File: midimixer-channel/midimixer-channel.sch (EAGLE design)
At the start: 97 parts, among them IC1 74LS595D, IC2 74LS595D, IC3 74LS595D, IC4 74165D, U1 LM1117IMPX-3.3/NOPB, Y1 8MHz 695-HCM49-8-U

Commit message: wip
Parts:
- removed JP3: (no value), microbuilder:HEADER-1X2ROUND
- removed X1: (no value), keves:TE-292304-1
- added USB: (no value), microbuilder:HEADER-1X4ROUND
- renumbered B1 to USR, B2 to RST
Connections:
- net 5.0V: no longer JP3.1
- net GND: now also USB.4; no longer JP3.2, X1SHIELD.S1, X1SHIELD.S2, X1_CONN.4
- net N$7: now also USB.2; no longer X1_CONN.2
- net N$8: now also USB.3; no longer X1_CONN.3
- net USB_VBUS: now also USB.1; no longer X1_CONN.1
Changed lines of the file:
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@@
 <part name="R12" library="microbuilder" deviceset="RESISTOR" device="_0603" value="10k"/>
 <part name="U$17" library="microbuilder" deviceset="GND" device=""/>
-<part name="X1" library="keves" deviceset="TE-292304-1" device=""/>
-<part name="U$18" library="microbuilder" deviceset="GND" device=""/>
 <part name="U$19" library="microbuilder" deviceset="GND" device=""/>
 <part name="R15" library="microbuilder" deviceset="RESISTOR" device="0603" value="22"/>
@@
 <part name="U$21" library="microbuilder" deviceset="3.3V" device=""/>
 <part name="U$22" library="microbuilder" deviceset="GND" device=""/>
-<part name="JP3" library="microbuilder" deviceset="HEADER-1X2" device="ROUND"/>
 <part name="JP4" library="microbuilder" deviceset="HEADER-1X2" device="ROUND"/>
-<part name="U$23" library="microbuilder" deviceset="GND" device=""/>
 <part name="U$24" library="microbuilder" deviceset="GND" device=""/>
-<part name="U$25" library="microbuilder" deviceset="5.0V" device=""/>
 <part name="U$26" library="microbuilder" deviceset="3.3V" device=""/>
 <part name="U1" library="microbuilder" deviceset="LM1117" device="SOT223-REFLOW" value="LM1117IMPX-3.3/NOPB"/>
@@
 <part name="C19" library="microbuilder" deviceset="CAP_CERAMIC" device="0603" value="0.1uF"/>
 <part name="U$31" library="microbuilder" deviceset="AVDD" device=""/>
-<part name="B2" library="microbuilder" deviceset="SWITCH_TACT_SMT" device=""/>
-<part name="B1" library="microbuilder" deviceset="SWITCH_TACT_SMT" device=""/>
+<part name="RST" library="microbuilder" deviceset="SWITCH_TACT_SMT" device=""/>
+<part name="USR" library="microbuilder" deviceset="SWITCH_TACT_SMT" device=""/>
 <part name="U$32" library="microbuilder" deviceset="GND" device=""/>
 <part name="U$33" library="microbuilder" deviceset="GND" device=""/>
@@
 <part name="U$36" library="microbuilder" deviceset="GND" device=""/>
 <part name="JP5" library="microbuilder" deviceset="HEADER-1X4" device="ROUND"/>
+<part name="USB" library="microbuilder" deviceset="HEADER-1X4" device="ROUND"/>
 </parts>
 <sheets>
@@
 <instance part="R12" gate="G$1" x="88.9" y="101.6"/>
 <instance part="U$17" gate="G$1" x="99.06" y="101.6" rot="R90"/>
-<instance part="X1" gate="_CONN" x="142.24" y="109.22"/>
-<instance part="X1" gate="SHIELD" x="142.24" y="111.76"/>
-<instance part="U$18" gate="G$1" x="144.78" y="96.52"/>
 <instance part="U$19" gate="G$1" x="137.16" y="96.52"/>
 <instance part="R15" gate="G$1" x="129.54" y="111.76"/>
@@
 <instance part="U$21" gate="G$1" x="167.64" y="116.84" rot="R90"/>
 <instance part="U$22" gate="G$1" x="167.64" y="106.68" rot="R270"/>
-<instance part="JP3" gate="G$1" x="180.34" y="93.98"/>
 <instance part="JP4" gate="G$1" x="180.34" y="81.28"/>
-<instance part="U$23" gate="G$1" x="165.1" y="93.98" rot="R270"/>
 <instance part="U$24" gate="G$1" x="165.1" y="81.28" rot="R270"/>
-<instance part="U$25" gate="G$1" x="170.18" y="96.52" rot="R90"/>
 <instance part="U$26" gate="G$1" x="170.18" y="83.82" rot="R90"/>
 <instance part="U1" gate="G$1" x="149.86" y="60.96"/>
@@
 <instance part="C19" gate="G$1" x="205.74" y="53.34"/>
 <instance part="U$31" gate="G$1" x="213.36" y="60.96" rot="R270"/>
-<instance part="B2" gate="G$1" x="147.32" y="27.94" rot="R90"/>
-<instance part="B1" gate="G$1" x="127" y="27.94" rot="R90"/>
+<instance part="RST" gate="G$1" x="147.32" y="27.94" rot="R90"/>
+<instance part="USR" gate="G$1" x="127" y="27.94" rot="R90"/>
 <instance part="U$32" gate="G$1" x="149.86" y="20.32"/>
 <instance part="U$33" gate="G$1" x="129.54" y="20.32"/>
@@
 <instance part="U$36" gate="G$1" x="5.08" y="0" rot="R90"/>
 <instance part="JP5" gate="A" x="-2.54" y="-2.54" rot="R180"/>
+<instance part="USB" gate="A" x="142.24" y="109.22"/>
 </instances>
 <busses>
@@
 </segment>
 <segment>
-<pinref part="X1" gate="SHIELD" pin="S1"/>
-<pinref part="U$18" gate="G$1" pin="GND"/>
-<pinref part="X1" gate="SHIELD" pin="S2"/>
-<wire x1="142.24" y1="99.06" x2="144.78" y2="99.06" width="0.2032" layer="91"/>
-<junction x="144.78" y="99.06"/>
-</segment>
-<segment>
-<pinref part="X1" gate="_CONN" pin="4"/>
 <pinref part="U$19" gate="G$1" pin="GND"/>
 <wire x1="139.7" y1="106.68" x2="137.16" y2="106.68" width="0.2032" layer="91"/>
 <wire x1="137.16" y1="106.68" x2="137.16" y2="99.06" width="0.2032" layer="91"/>
-</segment>
-<segment>
-<pinref part="JP3" gate="G$1" pin="2"/>
-<pinref part="U$23" gate="G$1" pin="GND"/>
-<wire x1="167.64" y1="93.98" x2="177.8" y2="93.98" width="0.1524" layer="91"/>
+<pinref part="USB" gate="A" pin="4"/>
 </segment>
 <segment>
@@
 </segment>
 <segment>
-<pinref part="B2" gate="G$1" pin="P1"/>
+<pinref part="RST" gate="G$1" pin="P1"/>
 <pinref part="U$32" gate="G$1" pin="GND"/>
-<pinref part="B2" gate="G$1" pin="P"/>
+<pinref part="RST" gate="G$1" pin="P"/>
 <wire x1="147.32" y1="22.86" x2="149.86" y2="22.86" width="0.2032" layer="91"/>
 <pinref part="C16" gate="G$1" pin="P$2"/>
@@
 </segment>
 <segment>
-<pinref part="B1" gate="G$1" pin="P1"/>
+<pinref part="USR" gate="G$1" pin="P1"/>
 <pinref part="U$33" gate="G$1" pin="GND"/>
-<pinref part="B1" gate="G$1" pin="P"/>
+<pinref part="USR" gate="G$1" pin="P"/>
 <wire x1="127" y1="22.86" x2="129.54" y2="22.86" width="0.2032" layer="91"/>
 <junction x="129.54" y="22.86"/>
@@
 <wire x1="154.94" y1="30.48" x2="154.94" y2="33.02" width="0.2032" layer="91"/>
 <wire x1="154.94" y1="33.02" x2="149.86" y2="33.02" width="0.2032" layer="91"/>
-<pinref part="B2" gate="G$1" pin="S1"/>
+<pinref part="RST" gate="G$1" pin="S1"/>
 <junction x="149.86" y="33.02"/>
 <wire x1="149.86" y1="33.02" x2="147.32" y2="33.02" width="0.2032" layer="91"/>
-<pinref part="B2" gate="G$1" pin="S"/>
+<pinref part="RST" gate="G$1" pin="S"/>
 <junction x="147.32" y="33.02"/>
 <wire x1="147.32" y1="33.02" x2="139.7" y2="33.02" width="0.2032" layer="91"/>
@@
 <net name="N$7" class="0">
 <segment>
-<pinref part="X1" gate="_CONN" pin="2"/>
 <pinref part="R15" gate="G$1" pin="2"/>
 <wire x1="139.7" y1="111.76" x2="134.62" y2="111.76" width="0.2032" layer="91"/>
+<pinref part="USB" gate="A" pin="2"/>
 </segment>
 </net>
 <net name="N$8" class="0">
 <segment>
-<pinref part="X1" gate="_CONN" pin="3"/>
 <pinref part="R16" gate="G$1" pin="2"/>
 <wire x1="139.7" y1="109.22" x2="134.62" y2="109.22" width="0.2032" layer="91"/>
+<pinref part="USB" gate="A" pin="3"/>
 </segment>
 </net>
@@
 <net name="USB_VBUS" class="0">
 <segment>
-<pinref part="X1" gate="_CONN" pin="1"/>
 <wire x1="139.7" y1="114.3" x2="132.08" y2="114.3" width="0.2032" layer="91"/>
 <label x="114.3" y="114.3" size="1.778" layer="95"/>
@@
 <wire x1="132.08" y1="121.92" x2="132.08" y2="114.3" width="0.2032" layer="91"/>
 <junction x="132.08" y="114.3"/>
+<pinref part="USB" gate="A" pin="1"/>
 </segment>
 <segment>
@@
 <pinref part="JP1" gate="A" pin="1"/>
 <wire x1="124.46" y1="121.92" x2="129.54" y2="121.92" width="0.2032" layer="91"/>
-</segment>
-<segment>
-<pinref part="JP3" gate="G$1" pin="1"/>
-<pinref part="U$25" gate="G$1" pin="5.0V"/>
-<wire x1="172.72" y1="96.52" x2="177.8" y2="96.52" width="0.1524" layer="91"/>
 </segment>
 <segment>
@@
 </segment>
 <segment>
-<pinref part="B1" gate="G$1" pin="S1"/>
+<pinref part="USR" gate="G$1" pin="S1"/>
 <wire x1="129.54" y1="33.02" x2="127" y2="33.02" width="0.2032" layer="91"/>
 <label x="116.84" y="33.02" size="1.778" layer="95"/>
-<pinref part="B1" gate="G$1" pin="S"/>
+<pinref part="USR" gate="G$1" pin="S"/>
 <junction x="127" y="33.02"/>
 <wire x1="127" y1="33.02" x2="119.38" y2="33.02" width="0.2032" layer="91"/>

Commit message: wip
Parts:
- added C26: 0.1uF, microbuilder:CAP_CERAMIC0603
- added IC5: 74165D, SparkFun-DigitalIC:74165D
- added R30, R31, R32, R33, R34, R35, R36, R37, R38: 10k, microbuilder:RESISTOR_0603
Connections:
- removed net DIN_TODO: BTN1.SW2_A, BTN1.SW2_B, C20.P$2
- removed net DIN_TODO2: BTN4.SW2_B, C23.P$2
- removed net N$36: BTN5.SW2_A, BTN5.SW2_B, C24.P$2
- removed net N$41: BTN3.SW2_A, BTN3.SW2_B, C22.P$2
- removed net N$46: BTN6.SW2_B, C25.P$2
- new net DIN_10: BTN1.SW2_A, BTN1.SW2_B, C20.P$2, IC5.B, R36.1
- new net DIN_11: BTN5.SW2_A, BTN5.SW2_B, C24.P$2, IC5.C, R35.1
- new net DIN_12: BTN4.SW2_B, C23.P$2, IC5.D, R34.1
- new net DIN_13: BTN3.SW2_A, BTN3.SW2_B, C22.P$2, IC5.E, R33.1
- new net DIN_14: BTN6.SW2_B, C25.P$2, IC5.F, R32.1
- new net DIN_15: IC5.G, R31.1
- new net DIN_16: IC5.H, R30.1
- new net DIN_9: BTN2.SW2_B, C21.P$2, IC5.A, R37.1
- net 3.3V: now also C26.P$2, IC5.VCC, R30.2, R31.2, R32.2, R33.2, R34.2, R35.2, R36.2, R37.2, R38.2
- net GND: now also C26.P$1, IC5.CLK_INH, IC5.GND
- net N$26: now also IC5.SER, R38.1; no longer BTN2.SW2_B, C21.P$2
- net N$28: now also IC5.QH
- net SPI2_CLK: now also IC5.CLK
- net SPI2_RC2: now also IC5.SH/!LD

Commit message: wip
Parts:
- added JP3: (no value), microbuilder:HEADER-1X3ROUND
- renumbered JP4 to PWR3.3V
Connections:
- removed net N$65: IC1.QH*
- new net UART_RX: CPU1.PC11/SDIO_D3, JP3.2
- new net UART_TX: CPU1.PC10/SDIO_D2, JP3.3
- net GND: now also JP3.1
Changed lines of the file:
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@@
 <part name="U$21" library="microbuilder" deviceset="3.3V" device=""/>
 <part name="U$22" library="microbuilder" deviceset="GND" device=""/>
-<part name="JP4" library="microbuilder" deviceset="HEADER-1X2" device="ROUND"/>
+<part name="PWR3.3V" library="microbuilder" deviceset="HEADER-1X2" device="ROUND"/>
 <part name="U$24" library="microbuilder" deviceset="GND" device=""/>
 <part name="U$26" library="microbuilder" deviceset="3.3V" device=""/>
@@
 <part name="R38" library="microbuilder" deviceset="RESISTOR" device="_0603" value="10k"/>
 <part name="U$47" library="microbuilder" deviceset="3.3V" device=""/>
+<part name="JP3" library="microbuilder" deviceset="HEADER-1X3" device="ROUND"/>
+<part name="U$51" library="microbuilder" deviceset="GND" device=""/>
 </parts>
 <sheets>
@@
 <instance part="U$21" gate="G$1" x="167.64" y="116.84" rot="R90"/>
 <instance part="U$22" gate="G$1" x="167.64" y="106.68" rot="R270"/>
-<instance part="JP4" gate="G$1" x="180.34" y="81.28"/>
+<instance part="PWR3.3V" gate="G$1" x="180.34" y="81.28"/>
 <instance part="U$24" gate="G$1" x="165.1" y="81.28" rot="R270"/>
 <instance part="U$26" gate="G$1" x="170.18" y="83.82" rot="R90"/>
@@
 <instance part="R38" gate="G$1" x="-121.92" y="-43.18" rot="R90"/>
 <instance part="U$47" gate="G$1" x="-121.92" y="-33.02"/>
+<instance part="JP3" gate="A" x="152.4" y="83.82"/>
+<instance part="U$51" gate="G$1" x="139.7" y="86.36" rot="R270"/>
 </instances>
 <busses>
@@
 </segment>
 <segment>
-<pinref part="JP4" gate="G$1" pin="1"/>
+<pinref part="PWR3.3V" gate="G$1" pin="1"/>
 <pinref part="U$26" gate="G$1" pin="3.3V"/>
 <wire x1="172.72" y1="83.82" x2="177.8" y2="83.82" width="0.1524" layer="91"/>
@@
 </segment>
 <segment>
-<pinref part="JP4" gate="G$1" pin="2"/>
+<pinref part="PWR3.3V" gate="G$1" pin="2"/>
 <pinref part="U$24" gate="G$1" pin="GND"/>
 <wire x1="167.64" y1="81.28" x2="177.8" y2="81.28" width="0.1524" layer="91"/>
@@
 <pinref part="IC5" gate="A" pin="CLK_INH"/>
 <pinref part="U$42" gate="G$1" pin="GND"/>
+</segment>
+<segment>
+<pinref part="JP3" gate="A" pin="1"/>
+<pinref part="U$51" gate="G$1" pin="GND"/>
+<wire x1="142.24" y1="86.36" x2="149.86" y2="86.36" width="0.1524" layer="91"/>
 </segment>
 </net>
@@
 </segment>
 </net>
-<net name="N$65" class="0">
-<segment>
-<pinref part="IC1" gate="A" pin="QH*"/>
-<wire x1="-71.12" y1="134.62" x2="-58.42" y2="134.62" width="0.2032" layer="91"/>
-<label x="-60.96" y="134.62" size="1.778" layer="95"/>
-</segment>
-</net>
 <net name="SPI2_MOSI" class="0">
 <segment>
@@
 </segment>
 </net>
+<net name="UART_TX" class="0">
+<segment>
+<pinref part="CPU1" gate="G$1" pin="PC10/SDIO_D2"/>
+<wire x1="81.28" y1="78.74" x2="83.82" y2="78.74" width="0.2032" layer="91"/>
+<label x="83.82" y="78.74" size="1.778" layer="95"/>
+</segment>
+<segment>
+<pinref part="JP3" gate="A" pin="3"/>
+<wire x1="149.86" y1="81.28" x2="129.54" y2="81.28" width="0.2032" layer="91"/>
+<label x="124.46" y="81.28" size="1.778" layer="95"/>
+</segment>
+</net>
+<net name="UART_RX" class="0">
+<segment>
+<pinref part="CPU1" gate="G$1" pin="PC11/SDIO_D3"/>
+<wire x1="81.28" y1="81.28" x2="83.82" y2="81.28" width="0.2032" layer="91"/>
+<label x="83.82" y="81.28" size="1.778" layer="95"/>
+</segment>
+<segment>
+<pinref part="JP3" gate="A" pin="2"/>
+<wire x1="149.86" y1="83.82" x2="129.54" y2="83.82" width="0.2032" layer="91"/>
+<label x="124.46" y="83.82" size="1.778" layer="95"/>
+</segment>
+</net>

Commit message: wip
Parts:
- renumbered JP1 to VBUS, JP2 to BUS1, JP3 to SER, JP5 to BUS2
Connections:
- net ADC0: now also POT2.S; no longer POT5.S
- net ADC1: now also POT4.S; no longer POT6.S
- net ADC2: now also POT6.S; no longer POT7.S
- net ADC3: now also POT1.S; no longer POT4.S
- net ADC5: now also POT5.S; no longer POT2.S
- net ADC6: now also POT7.S; no longer POT1.S
- net BTN_LED1: now also BTN2.LED1+; no longer BTN3.LED1+
- net BTN_LED10: now also BTN6.LED2+; no longer BTN5.LED2+
- net BTN_LED11: now also BTN3.LED1+; no longer BTN6.LED1+
- net BTN_LED12: now also BTN3.LED2+; no longer BTN6.LED2+
- net BTN_LED2: now also BTN2.LED2+; no longer BTN3.LED2+
- net BTN_LED3: now also BTN1.LED1+; no longer BTN2.LED1+
- net BTN_LED4: now also BTN1.LED2+; no longer BTN2.LED2+
- net BTN_LED5: now also BTN4.LED1+; no longer BTN1.LED1+
- net BTN_LED6: now also BTN6.LED1+; no longer BTN5.LED1+
- net BTN_LED7: now also BTN5.LED1+; no longer BTN4.LED1+
- net BTN_LED8: now also BTN5.LED2+; no longer BTN4.LED2+
- net BTN_LED9: now also BTN4.LED2+; no longer BTN1.LED2+
- net DIN_10: now also BTN4.SW2_A, BTN4.SW2_B; no longer BTN1.SW2_A, BTN1.SW2_B
- net DIN_11: now also BTN6.SW2_A, BTN6.SW2_B; no longer BTN5.SW2_A, BTN5.SW2_B
- net DIN_12: now also BTN5.SW2_B; no longer BTN4.SW2_B
- net DIN_13: now also BTN2.SW2_A, BTN2.SW2_B; no longer BTN3.SW2_A, BTN3.SW2_B
- net DIN_14: now also BTN3.SW2_B; no longer BTN6.SW2_B
- net DIN_9: now also BTN1.SW2_B; no longer BTN2.SW2_B
- net GND: now also BTN2.SW1_A, BTN4.SW1_A, BTN6.SW1_A; no longer BTN1.SW1_A, BTN3.SW1_A, BTN5.SW1_A
- net N$10: now also BTN4.LED2-; no longer BTN1.LED2-
- net N$24: now also BTN1.LED1-; no longer BTN2.LED1-
- net N$25: now also BTN1.LED2-; no longer BTN2.LED2-
- net N$29: now also BTN5.LED1-; no longer BTN4.LED1-
- net N$30: now also BTN5.LED2-; no longer BTN4.LED2-
- net N$34: now also BTN6.LED1-; no longer BTN5.LED1-
- net N$35: now also BTN6.LED2-; no longer BTN5.LED2-
- net N$39: now also BTN2.LED1-; no longer BTN3.LED1-
- net N$40: now also BTN2.LED2-; no longer BTN3.LED2-
- net N$44: now also BTN3.LED1-; no longer BTN6.LED1-
- net N$45: now also BTN3.LED2-; no longer BTN6.LED2-
- net N$9: now also BTN4.LED1-; no longer BTN1.LED1-
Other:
- moved on the sheet: BTN1, BTN2, BTN3, BTN4, BTN5, BTN6, POT1, POT2, POT4, POT5, POT6, POT7

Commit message: reviving midimixer
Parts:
- added H5, H6: STAND-OFF, SparkFun-Electromechanical:STAND-OFF
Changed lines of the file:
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@@
 <?xml version="1.0" encoding="utf-8"?>
 <!DOCTYPE eagle SYSTEM "eagle.dtd">
-<eagle version="7.5.0">
+<eagle version="7.6.0">
 <drawing>
 <settings>
@@
 <part name="SER" library="microbuilder" deviceset="HEADER-1X3" device="ROUND"/>
 <part name="U$51" library="microbuilder" deviceset="GND" device=""/>
+<part name="H5" library="SparkFun-Electromechanical" deviceset="STAND-OFF" device=""/>
+<part name="H6" library="SparkFun-Electromechanical" deviceset="STAND-OFF" device=""/>
 </parts>
 <sheets>
@@
 <instance part="SER" gate="A" x="152.4" y="83.82"/>
 <instance part="U$51" gate="G$1" x="139.7" y="86.36" rot="R270"/>
+<instance part="H5" gate="G$1" x="177.8" y="139.7"/>
+<instance part="H6" gate="G$1" x="182.88" y="142.24"/>
 </instances>
 <busses>

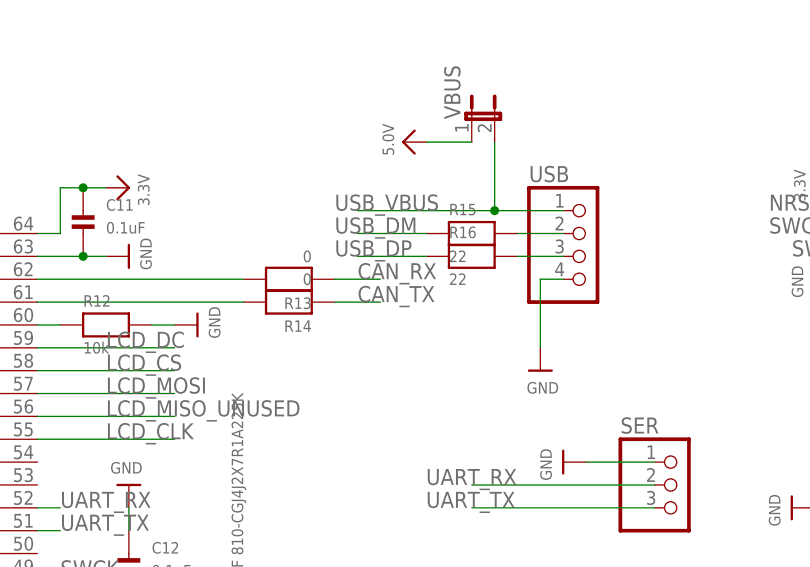
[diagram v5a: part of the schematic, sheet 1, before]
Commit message: fix can tx<->rx (flip them)
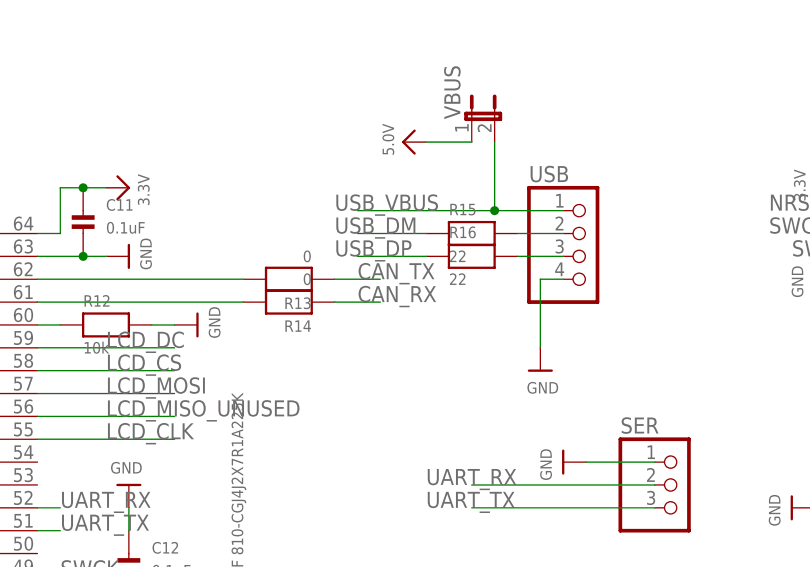
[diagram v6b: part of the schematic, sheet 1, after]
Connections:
- net CAN_RX: now also R14.1; no longer R13.1
- net CAN_TX: now also R13.1; no longer R14.1
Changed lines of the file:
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@@
 <?xml version="1.0" encoding="utf-8"?>
 <!DOCTYPE eagle SYSTEM "eagle.dtd">
-<eagle version="7.6.0">
+<eagle version="7.2.0">
 <drawing>
 <settings>
@@
 <net name="CAN_TX" class="0">
 <segment>
+<pinref part="D2" gate="G$1" pin="TXD"/>
+<wire x1="43.18" y1="-2.54" x2="27.94" y2="-2.54" width="0.2032" layer="91"/>
+<label x="27.94" y="-2.54" size="1.778" layer="95"/>
+</segment>
+<segment>
+<pinref part="R13" gate="G$1" pin="1"/>
+<wire x1="114.3" y1="106.68" x2="119.38" y2="106.68" width="0.2032" layer="91"/>
+<label x="116.84" y="106.68" size="1.778" layer="95"/>
+</segment>
+</net>
+<net name="CAN_RX" class="0">
+<segment>
+<pinref part="D2" gate="G$1" pin="RXD"/>
+<wire x1="43.18" y1="-7.62" x2="27.94" y2="-7.62" width="0.2032" layer="91"/>
+<label x="27.94" y="-7.62" size="1.778" layer="95"/>
+</segment>
+<segment>
 <pinref part="R14" gate="G$1" pin="1"/>
 <wire x1="114.3" y1="104.14" x2="119.38" y2="104.14" width="0.2032" layer="91"/>
 <label x="116.84" y="104.14" size="1.778" layer="95"/>
 </segment>
-<segment>
-<pinref part="D2" gate="G$1" pin="TXD"/>
-<wire x1="43.18" y1="-2.54" x2="27.94" y2="-2.54" width="0.2032" layer="91"/>
-<label x="27.94" y="-2.54" size="1.778" layer="95"/>
-</segment>
-</net>
-<net name="CAN_RX" class="0">
-<segment>
-<pinref part="D2" gate="G$1" pin="RXD"/>
-<wire x1="43.18" y1="-7.62" x2="27.94" y2="-7.62" width="0.2032" layer="91"/>
-<label x="27.94" y="-7.62" size="1.778" layer="95"/>
-</segment>
-<segment>
-<pinref part="R13" gate="G$1" pin="1"/>
-<wire x1="114.3" y1="106.68" x2="119.38" y2="106.68" width="0.2032" layer="91"/>
-<label x="116.84" y="106.68" size="1.778" layer="95"/>
-</segment>
-</net>
+</net>

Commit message: wip
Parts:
- D2: value SN65HVD230 -> SN65HVD232
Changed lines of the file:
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@@
 <part name="R2" library="microbuilder" deviceset="RESISTOR" device="_0603" value="10k"/>
 <part name="U$93" library="microbuilder" deviceset="3.3V" device=""/>
-<part name="D2" library="omc" deviceset="SN65HVD230" device=""/>
+<part name="D2" library="omc" deviceset="SN65HVD230" device="" value="SN65HVD232"/>
 <part name="C10" library="microbuilder" deviceset="CAP_CERAMIC" device="0603" value="0.1uF"/>
 <part name="U$94" library="microbuilder" deviceset="GND" device=""/>
